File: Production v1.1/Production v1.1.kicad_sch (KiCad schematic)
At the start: 28 parts, among them IC1 MAX3323EEUE+T, IC2 AP7375-33SA-7, J1 530480510, J2 530480410, J3 USB4085-GF-A_REVB, U2 ADR02AUJZ-REEL7, U3 ATSAMD21G18A-AUT, Y1 32.768, 12.5pF

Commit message: Solid v1.1 attempt, but going to start over
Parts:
- removed Y1: 32.768, 12.5pF, Crystal:Crystal_SMD_3215-2Pin_3.2x1.5mm, symbol Device:Crystal_Small
- added Y1: ECS-.327-12.5-1210-TR, ECS__327_12_5_1210_TR:XTAL_ECS-.327-12.5-1210-TR, symbol ECS-.327-12.5-1210-TR:ECS-.327-12.5-1210-TR
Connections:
- net ROUT1: now also U3.30 (PA21); no longer U3.29 (PA20)
- net TIN1: now also U3.29 (PA20); no longer U3.30 (PA21)
- net at C6.2, U3.1 (PA00): now also Y1.2
- net at C7.2, U3.2 (PA01): now also Y1.1

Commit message: Better v1.1, but I can do better
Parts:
- R1, R2, R3, R5, R8: footprint Resistor_SMD:R_0603_1608Metric -> Resistor_SMD:R_0201_0603Metric
- RESET1: footprint Button_Switch_SMD:SW_SPST_B3U-1000P -> Button_Switch_SMD:SW_SPST_B3U-3000P
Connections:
- net RUN: now also U3.24 (PA15); no longer U3.39 (PA27)
- net ZSIG: now also U3.16 (PA11); no longer U3.47 (PB02)

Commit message: Components are all moved to the bottom layer, top is ground
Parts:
- R1, R2, R3, R5, R8: footprint Resistor_SMD:R_0201_0603Metric -> Resistor_SMD:R_0603_1608Metric
- renumbered RESET1 to S3
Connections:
- net RXLED is gone; now on net SETLED: U3.48 (PB03)
- net OLED_CS: now also U3.9 (PA04); no longer U3.7 (PB08)
- net OLED_DC: now also U3.7 (PB08); no longer U3.9 (PA04)
- net RUN: now also U3.39 (PA27); no longer U3.24 (PA15)
- net SETBTN: now also U3.3 (PA02); no longer U3.14 (PA09)
- net SETLED: no longer U3.13 (PA08)
- net SOFTBTN: now also U3.14 (PA09); no longer U3.3 (PA02)
- net ZSIG: now also U3.47 (PB02); no longer U3.16 (PA11)
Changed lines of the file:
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@@
 	(wire
 		(pts
+			(xy 256.54 106.68) (xy 260.35 106.68)
+		)
+		(stroke
+			(width 0)
+			(type default)
+		)
+	)
+	(wire
+		(pts
 			(xy 67.31 144.78) (xy 69.85 144.78)
 		)
@@
 	(wire
 		(pts
-			(xy 256.54 93.98) (xy 260.35 93.98)
-		)
-		(stroke
-			(width 0)
-			(type default)
-		)
-	)
-	(wire
-		(pts
 			(xy 269.24 20.32) (xy 269.24 33.02)
 		)
@@
 	(wire
 		(pts
-			(xy 226.06 81.28) (xy 231.14 81.28)
-		)
-		(stroke
-			(width 0)
-			(type default)
-		)
-	)
-	(wire
-		(pts
 			(xy 215.9 143.51) (xy 219.71 143.51)
 		)
@@
 		)
 	)
-	(global_label "RXLED"
-		(shape input)
-		(at 260.35 93.98 0)
-		(fields_autoplaced yes)
-		(effects
-			(font
-				(size 1.27 1.27)
-			)
-			(justify left)
-		)
-		(property "Intersheetrefs" "${INTERSHEET_REFS}"
-			(at 269.2618 93.98 0)
-			(effects
-				(font
-					(size 1.27 1.27)
-				)
-				(justify left)
-				(hide yes)
-			)
-		)
-	)
 	(global_label "MOSI"
 		(shape input)
@@
 	(global_label "SETLED"
 		(shape input)
-		(at 231.14 96.52 180)
+		(at 256.54 93.98 0)
 		(fields_autoplaced yes)
 		(effects
@@
 				(size 1.27 1.27)
 			)
-			(justify right)
+			(justify left)
 		)
 		(property "Intersheetrefs" "${INTERSHEET_REFS}"
-			(at 221.3816 96.52 0)
+			(at 266.2984 93.98 0)
 			(effects
 				(font
 					(size 1.27 1.27)
 				)
-				(justify right)
+				(justify left)
 				(hide yes)
 			)
@@
 	(global_label "SOFTBTN"
 		(shape input)
-		(at 226.06 81.28 180)
+		(at 231.14 99.06 180)
 		(fields_autoplaced yes)
 		(effects
@@
 		)
 		(property "Intersheetrefs" "${INTERSHEET_REFS}"
-			(at 214.9105 81.28 0)
+			(at 219.9905 99.06 0)
 			(effects
 				(font
@@
 	(global_label "SETBTN"
 		(shape input)
-		(at 231.14 99.06 180)
+		(at 231.14 81.28 180)
 		(fields_autoplaced yes)
 		(effects
@@
 		)
 		(property "Intersheetrefs" "${INTERSHEET_REFS}"
-			(at 221.2606 99.06 0)
+			(at 221.2606 81.28 0)
 			(effects
 				(font
@@
 	(global_label "ZSIG"
 		(shape input)
-		(at 231.14 104.14 180)
+		(at 256.54 96.52 0)
 		(fields_autoplaced yes)
 		(effects
@@
 				(size 1.27 1.27)
 			)
-			(justify right)
+			(justify left)
 		)
 		(property "Intersheetrefs" "${INTERSHEET_REFS}"
-			(at 223.861 104.14 0)
+			(at 263.819 96.52 0)
 			(effects
 				(font
 					(size 1.27 1.27)
 				)
-				(justify right)
+				(justify left)
 				(hide yes)
 			)
@@
 	(global_label "RUN"
 		(shape input)
-		(at 231.14 114.3 180)
+		(at 260.35 106.68 0)
 		(fields_autoplaced yes)
 		(effects
@@
 				(size 1.27 1.27)
 			)
-			(justify right)
+			(justify left)
 		)
 		(property "Intersheetrefs" "${INTERSHEET_REFS}"
-			(at 224.2238 114.3 0)
+			(at 267.2662 106.68 0)
 			(effects
 				(font
 					(size 1.27 1.27)
 				)
-				(justify right)
+				(justify left)
 				(hide yes)
 			)
@@
 	(global_label "OLED_DC"
 		(shape input)
-		(at 231.14 86.36 180)
+		(at 256.54 91.44 0)
 		(fields_autoplaced yes)
 		(effects
@@
 				(size 1.27 1.27)
 			)
-			(justify right)
+			(justify left)
 		)
 		(property "Intersheetrefs" "${INTERSHEET_REFS}"
-			(at 219.8696 86.36 0)
+			(at 267.8104 91.44 0)
 			(effects
 				(font
 					(size 1.27 1.27)
 				)
-				(justify right)
+				(justify left)
 				(hide yes)
 			)
@@
 	(global_label "OLED_CS"
 		(shape input)
-		(at 256.54 91.44 0)
+		(at 231.14 86.36 180)
 		(fields_autoplaced yes)
 		(effects
@@
 				(size 1.27 1.27)
 			)
-			(justify left)
+			(justify right)
 		)
 		(property "Intersheetrefs" "${INTERSHEET_REFS}"
-			(at 267.7499 91.44 0)
+			(at 219.9301 86.36 0)
 			(effects
 				(font
 					(size 1.27 1.27)
 				)
-				(justify left)
+				(justify right)
 				(hide yes)
 			)
@@
 			)
 		)
-		(property "Footprint" "Resistor_SMD:R_0201_0603Metric"
+		(property "Footprint" "Resistor_SMD:R_0603_1608Metric"
 			(at 104.14 156.718 90)
 			(effects
@@
 			)
 		)
-		(property "Footprint" "Resistor_SMD:R_0201_0603Metric"
+		(property "Footprint" "Resistor_SMD:R_0603_1608Metric"
 			(at 104.14 154.178 90)
 			(effects
@@
 			)
 		)
-		(property "Footprint" "Resistor_SMD:R_0201_0603Metric"
+		(property "Footprint" "Resistor_SMD:R_0603_1608Metric"
 			(at 201.93 145.288 90)
 			(effects
@@
 		(dnp no)
 		(fields_autoplaced yes)
-		(property "Reference" "RESET1"
+		(property "Reference" "S3"
 			(at 58.42 106.68 0)
 			(effects
@@
 			(project "Production v1.1"
 				(path "/36880c03-5560-4777-bc12-f18c70ba2db4"
-					(reference "RESET1")
+					(reference "S3")
 					(unit 1)
 				)
@@
 			)
 		)
-		(property "Footprint" "Resistor_SMD:R_0201_0603Metric"
+		(property "Footprint" "Resistor_SMD:R_0603_1608Metric"
 			(at 151.13 145.288 90)
 			(effects
@@
 			)
 		)
-		(property "Footprint" "Resistor_SMD:R_0201_0603Metric"
+		(property "Footprint" "Resistor_SMD:R_0603_1608Metric"
 			(at 167.64 145.288 90)
 			(effects

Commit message: Solid v1.1, but I want to change how the oled is mounted.
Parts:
- C13: value 10uF,10V+ -> 22uF,10V+; Part Number CL05A106MP6NUN8 -> GRM158R61A226ME15D; URL https://www.digikey.com/en/products/detail/samsung-electro-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 -> https://www.digikey.com/en/products/detail/murata-electroni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
- C4: value 1uF,60V+ -> 2.2uF,100V; Part Number GRM21BC72A105KE01L -> C2012X7R2A225K125AC; URL https://www.digikey.com/en/products/detail/murata-electroni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 -> https://www.digikey.com/en/products/detail/tdk-corporation/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
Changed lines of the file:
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@@
 			)
 		)
-		(property "Value" "1uF,60V+"
+		(property "Value" "2.2uF,100V"
 			(at 119.38 44.4499 0)
 			(effects
@@
 			)
 		)
-		(property "Part Number" "GRM21BC72A105KE01L"
+		(property "Part Number" "C2012X7R2A225K125AC"
 			(at 115.57 43.18 0)
 			(effects
@@
 			)
 		)
-		(property "URL" "https://www.digikey.com/en/products/detail/murata-electronics/GRM21BC72A105KE01L/6606093"
+		(property "URL" "https://www.digikey.com/en/products/detail/tdk-corporation/C2012X7R2A225K125AC/20482638"
 			(at 115.57 43.18 0)
 			(effects
@@
 			)
 		)
-		(property "Value" "10uF,10V+"
+		(property "Value" "22uF,10V+"
 			(at 180.34 49.5299 0)
 			(effects
@@
 			)
 		)
-		(property "Part Number" "CL05A106MP6NUN8"
+		(property "Part Number" "GRM158R61A226ME15D"
 			(at 176.53 48.26 0)
 			(effects
@@
 			)
 		)
-		(property "URL" "https://www.digikey.com/en/products/detail/samsung-electro-mechanics/CL05A106MP6NUN8/10478957"
+		(property "URL" "https://www.digikey.com/en/products/detail/murata-electronics/GRM158R61A226ME15D/16033379"
 			(at 176.53 48.26 0)
 			(effects

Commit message: v1.1 sent for assembly
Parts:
- R1, R2, R3, R5, R8: footprint Resistor_SMD:R_0603_1608Metric -> Resistor_SMD:R_0201_0603Metric
- S1: value FSM12JH -> TL6100DF300QP; footprint FSM10JH:FSM4JH -> TL6100DF300QP:TL6100DF160QP; symbol FSM10JH:FSM10JH -> TL6100DF300QP:TL6100AF300QP; Manufacturer_Name TE Connectivity -> E-Switch; Manufacturer_Part_Number FSM10JH -> TL6100DF300QP; Mouser Part Number 506-FSM10JH -> (none); Mouser Price/Stock https://www.mouser.co.uk/ProductDetail/TE-Connectivity-PB/F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 -> (none); Part Number 1-1825910-4 -> TL6100DF300QP; URL https://www.digikey.com/en/products/detail/te-connectivity-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 -> https://www.digikey.com/en/products/detail/e-switch/TL6100D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
- S2: value FSM12JH -> TL6100DF300QP; footprint FSM10JH:FSM4JH -> TL6100DF300QP:TL6100DF160QP; symbol FSM10JH:FSM10JH -> TL6100DF300QP:TL6100AF300QP; Height (none) -> 10.25; Manufacturer_Name TE Connectivity -> E-Switch; Manufacturer_Part_Number FSM10JH -> TL6100DF300QP; Mouser Part Number 506-FSM10JH -> (none); Mouser Price/Stock https://www.mouser.co.uk/ProductDetail/TE-Connectivity-PB/F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 -> (none); Part Number 1-1825910-4 -> TL6100DF300QP; URL https://www.digikey.com/en/products/detail/te-connectivity-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 -> https://www.digikey.com/en/products/detail/e-switch/TL6100D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
- S3: value B3U-1000P -> B3U-3000P; DK_Datasheet_Link https://omronfs.omron.com/en_US/ecb/products/pdf/en-b3u.pdf -> (none); DK_Detail_Page /product-detail/en/omron-electronics-inc-emc-div/B3U-1000P/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 -> (none); MPN B3U-1000P -> B3U-3000P; Part Number B3U-1000P -> B3U-3000P; URL https://www.digikey.com/en/products/detail/omron-electronics-inc-emc-div/B3U-1000P/1534338 -> https://www.digikey.com/en/products/detail/omron-electronics-inc-emc-div/B3U-3000P/1534340
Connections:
- net GND: now also S1.1, S2.1; no longer S1.3, S2.3
- net SETBTN: now also S1.3; no longer S1.1
- net SOFTBTN: now also S2.3; no longer S2.1
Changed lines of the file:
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@@
 			)
 		)
-		(property "Footprint" "Resistor_SMD:R_0603_1608Metric"
+		(property "Footprint" "Resistor_SMD:R_0201_0603Metric"
 			(at 104.14 156.718 90)
 			(effects
@@
 			)
 		)
-		(property "Footprint" "Resistor_SMD:R_0603_1608Metric"
+		(property "Footprint" "Resistor_SMD:R_0201_0603Metric"
 			(at 104.14 154.178 90)
 			(effects
@@
 	)
 	(symbol
-		(lib_id "FSM10JH:FSM10JH")
+		(lib_id "TL6100DF300QP:TL6100AF300QP")
 		(at 46.99 127 0)
 		(unit 1)
@@
 			)
 		)
-		(property "Value" "FSM12JH"
+		(property "Value" "TL6100DF300QP"
 			(at 57.15 121.92 0)
 			(effects
@@
 			)
 		)
-		(property "Footprint" "FSM10JH:FSM4JH"
+		(property "Footprint" "TL6100DF300QP:TL6100DF160QP"
 			(at 63.5 221.92 0)
 			(effects
@@
 			)
 		)
-		(property "Datasheet" "http://www.te.com/commerce/DocumentDelivery/DDEController?Action=showdoc&DocId=Customer+Drawing%7F1825910%7FC10%7Fpdf%7FEnglish%7FENG_CD_1825910_C10.pdf%7F1-1825910-8"
+		(property "Datasheet" "https://configured-product-images.s3.amazonaws.com/2D/specs/TL6100AF300QP.pdf"
 			(at 63.5 321.92 0)
 			(effects
@@
 			)
 		)
-		(property "Description" "6x6mm tactile switch,7.3mm H 1.6N White Button Tactile Switch, SPST 50 mA@ 24 V dc 3.7mm"
+		(property "Description" "TACT, 50mA, 12VDC SPST-NO, Off-(On) Through Hole"
 			(at 46.99 127 0)
 			(effects
@@
 			)
 		)
-		(property "Height" ""
-			(at 63.5 521.92 0)
+		(property "Manufacturer_Name" "E-Switch"
+			(at 63.5 621.92 0)
 			(effects
 				(font
@@
 			)
 		)
-		(property "Mouser Part Number" "506-FSM10JH"
-			(at 63.5 621.92 0)
+		(property "Manufacturer_Part_Number" "TL6100DF300QP"
+			(at 63.5 721.92 0)
 			(effects
 				(font
@@
 			)
 		)
-		(property "Mouser Price/Stock" "https://www.mouser.co.uk/ProductDetail/TE-Connectivity-PB/FSM10JH?qs=g%252BEszo6zu8Mx34MmAD%2FJ0A%3D%3D"
-			(at 63.5 721.92 0)
-			(effects
-				(font
-					(size 1.27 1.27)
-				)
-				(justify left top)
-				(hide yes)
-			)
-		)
-		(property "Manufacturer_Name" "TE Connectivity"
-			(at 63.5 821.92 0)
-			(effects
-				(font
-					(size 1.27 1.27)
-				)
-				(justify left top)
-				(hide yes)
-			)
-		)
-		(property "Manufacturer_Part_Number" "FSM10JH"
-			(at 63.5 921.92 0)
-			(effects
-				(font
-					(size 1.27 1.27)
-				)
-				(justify left top)
-				(hide yes)
-			)
-		)
-		(property "Part Number" "1-1825910-4"
+		(property "Part Number" "TL6100DF300QP"
 			(at 46.99 127 0)
 			(effects
@@
 			)
 		)
-		(property "URL" "https://www.digikey.com/en/products/detail/te-connectivity-alcoswitch-switches/1-1825910-4/1632539"
+		(property "URL" "https://www.digikey.com/en/products/detail/e-switch/TL6100DF300QP/659874"
 			(at 46.99 127 0)
 			(effects
@@
 			)
 		)
-		(property "Footprint" "Resistor_SMD:R_0603_1608Metric"
+		(property "Footprint" "Resistor_SMD:R_0201_0603Metric"
 			(at 201.93 145.288 90)
 			(effects
@@
 			)
 		)
-		(property "Value" "B3U-1000P"
+		(property "Value" "B3U-3000P"
 			(at 58.42 109.22 0)
 			(effects
@@
 			)
 		)
-		(property "MPN" "B3U-1000P"
+		(property "MPN" "B3U-3000P"
 			(at 63.5 101.6 0)
 			(effects
@@
 			)
 		)
-		(property "DK_Datasheet_Link" "https://omronfs.omron.com/en_US/ecb/products/pdf/en-b3u.pdf"
-			(at 63.5 93.98 0)
-			(effects
-				(font
-					(size 1.524 1.524)
-				)
-				(justify left)
-				(hide yes)
-			)
-		)
-		(property "DK_Detail_Page" "/product-detail/en/omron-electronics-inc-emc-div/B3U-1000P/SW1020CT-ND/1534357"
-			(at 63.5 91.44 0)
-			(effects
-				(font
-					(size 1.524 1.524)
-				)
-				(justify left)
-				(hide yes)
-			)
-		)
 		(property "Manufacturer" "Omron Electronics Inc-EMC Div"
 			(at 63.5 86.36 0)
@@
 			)
 		)
-		(property "Part Number" "B3U-1000P"
+		(property "Part Number" "B3U-3000P"
 			(at 58.42 114.3 0)
 			(effects
@@
 			)
 		)
-		(property "URL" "https://www.digikey.com/en/products/detail/omron-electronics-inc-emc-div/B3U-1000P/1534338"
+		(property "URL" "https://www.digikey.com/en/products/detail/omron-electronics-inc-emc-div/B3U-3000P/1534340"
+			(at 58.42 114.3 0)
+			(effects
+				(font
+					(size 1.27 1.27)
+				)
+				(hide yes)
+			)
+		)
+		(property "Field14" ""
 			(at 58.42 114.3 0)
 			(effects
@@
 			)
 		)
-		(property "Footprint" "Resistor_SMD:R_0603_1608Metric"
+		(property "Footprint" "Resistor_SMD:R_0201_0603Metric"
 			(at 151.13 145.288 90)
 			(effects
@@
 			)
 		)
-		(property "Footprint" "Resistor_SMD:R_0603_1608Metric"
+		(property "Footprint" "Resistor_SMD:R_0201_0603Metric"
 			(at 167.64 145.288 90)
 			(effects
@@
 	)
 	(symbol
-		(lib_id "FSM10JH:FSM10JH")
+		(lib_id "TL6100DF300QP:TL6100AF300QP")
 		(at 46.99 142.24 0)
 		(unit 1)
@@
 			)
 		)
-		(property "Value" "FSM12JH"
+		(property "Value" "TL6100DF300QP"
 			(at 57.15 137.16 0)
 			(effects
@@
 			)
 		)
-		(property "Footprint" "FSM10JH:FSM4JH"
+		(property "Footprint" "TL6100DF300QP:TL6100DF160QP"
 			(at 63.5 237.16 0)
 			(effects
@@
 			)
 		)
-		(property "Datasheet" "http://www.te.com/commerce/DocumentDelivery/DDEController?Action=showdoc&DocId=Customer+Drawing%7F1825910%7FC10%7Fpdf%7FEnglish%7FENG_CD_1825910_C10.pdf%7F1-1825910-8"
+		(property "Datasheet" "https://configured-product-images.s3.amazonaws.com/2D/specs/TL6100AF300QP.pdf"
 			(at 63.5 337.16 0)
 			(effects
@@
 			)
 		)
-		(property "Description" "6x6mm tactile switch,7.3mm H 1.6N White Button Tactile Switch, SPST 50 mA@ 24 V dc 3.7mm"
+		(property "Description" "TACT, 50mA, 12VDC SPST-NO, Off-(On) Through Hole"
 			(at 46.99 142.24 0)
 			(effects
@@
 			)
 		)
-		(property "Height" ""
+		(property "Height" "10.25"
 			(at 63.5 537.16 0)
 			(effects
@@
 			)
 		)
-		(property "Mouser Part Number" "506-FSM10JH"
+		(property "Manufacturer_Name" "E-Switch"
 			(at 63.5 637.16 0)
 			(effects
@@
 			)
 		)
-		(property "Mouser Price/Stock" "https://www.mouser.co.uk/ProductDetail/TE-Connectivity-PB/FSM10JH?qs=g%252BEszo6zu8Mx34MmAD%2FJ0A%3D%3D"
+		(property "Manufacturer_Part_Number" "TL6100DF300QP"
 			(at 63.5 737.16 0)
 			(effects
@@
 			)
 		)
-		(property "Manufacturer_Name" "TE Connectivity"
-			(at 63.5 837.16 0)
-			(effects
-				(font
-					(size 1.27 1.27)
-				)
-				(justify left top)
-				(hide yes)
-			)
-		)
-		(property "Manufacturer_Part_Number" "FSM10JH"
-			(at 63.5 937.16 0)
-			(effects
-				(font
-					(size 1.27 1.27)
-				)
-				(justify left top)
-				(hide yes)
-			)
-		)
-		(property "Part Number" "1-1825910-4"
+		(property "Part Number" "TL6100DF300QP"
 			(at 46.99 142.24 0)
 			(effects
@@
 			)
 		)
-		(property "URL" "https://www.digikey.com/en/products/detail/te-connectivity-alcoswitch-switches/1-1825910-4/1632539"
+		(property "URL" "https://www.digikey.com/en/products/detail/e-switch/TL6100DF300QP/659874"
 			(at 46.99 142.24 0)
 			(effects

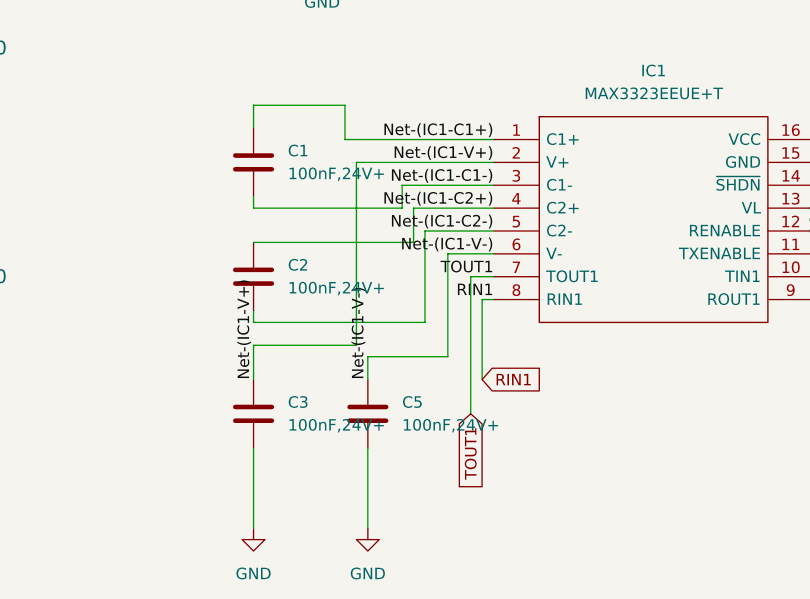
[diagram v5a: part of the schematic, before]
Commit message: Updated v1.1 and re-ordered
One net was not connected
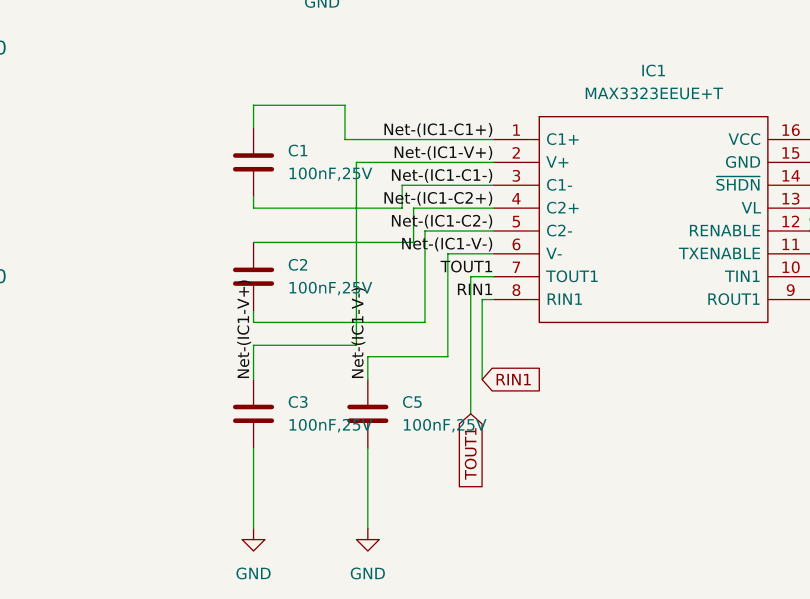
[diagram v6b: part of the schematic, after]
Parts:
- C1, C2, C3, C5: value 100nF,24V+ -> 100nF,25V
- IC1: Height 4.572 -> (none); Manufacturer_Name Analog Devices -> (none); Manufacturer_Part_Number MAX3323EEPE+ -> (none); Mouser Part Number 700-MAX3323EEPE -> (none); Mouser Price/Stock https://www.mouser.co.uk/ProductDetail/Analog-Devices-Maxim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 -> (none)
- IC2: Height 1.1 -> (none); Manufacturer_Name Diodes Incorporated -> (none); Manufacturer_Part_Number AP7375-33SA-7 -> (none); Mouser Part Number 621-AP7375-33SA-7 -> (none); Mouser Price/Stock https://www.mouser.co.uk/ProductDetail/Diodes-Incorporated/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 -> (none)
- J3: MANUFACTURER Global Connector Technology -> (none); MAXIMUM_PACKAGE_HEIGHT 3.16mm -> (none); PARTREV B -> (none); SNAPEDA_PN USB4085-GF-A -> (none); STANDARD Manufacturer Recommendations -> (none)
- R1, R2: Part Number ESR03EZPJ512 -> ERJ-1GNF5101C; URL https://www.digikey.com/en/products/detail/rohm-semiconduct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 -> https://www.digikey.com/en/products/detail/panasonic-electr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
- R3: Part Number RC0603FR-074K7L -> ERJ-1GNF4701C; URL https://www.digikey.com/en/products/detail/yageo/RC0603FR-0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 -> https://www.digikey.com/en/products/detail/panasonic-electr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
- R5: Part Number RC0603FR-073K3L -> ERJ-1GNF3301C; URL https://www.digikey.com/en/products/detail/yageo/RC0603FR-0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 -> https://www.digikey.com/en/products/detail/panasonic-electr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
- R8: Part Number RC0603FR-0764R9L -> ERJ-1GNF64R9C; URL https://www.digikey.com/en/products/detail/yageo/RC0603FR-0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 -> https://www.digikey.com/en/products/detail/panasonic-electr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
- S1: Manufacturer_Name E-Switch -> (none); Manufacturer_Part_Number TL6100DF300QP -> (none)
- S2: Height 10.25 -> (none); Manufacturer_Name E-Switch -> (none); Manufacturer_Part_Number TL6100DF300QP -> (none)
- S3: Category Switches -> (none); Family Tactile Switches -> (none); MPN B3U-3000P -> (none); Manufacturer Omron Electronics Inc-EMC Div -> (none); Status Active -> (none)
- U3: Category Integrated Circuits (ICs) -> (none); DK_Datasheet_Link http://www.microchip.com/mymicrochip/filehandler.aspx?ddocn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 -> (none); DK_Detail_Page /product-detail/en/microchip-technology/ATSAMD21G18A-AUT/AT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 -> (none); Family Embedded - Microcontrollers -> (none); MPN ATSAMD21G18A-AUT -> (none); Manufacturer Microchip Technology -> (none); Status Active -> (none)
- Y1: MANUFACTURER ESC Inc. -> (none); STANDARD Manufacturer Recommendations -> (none)
